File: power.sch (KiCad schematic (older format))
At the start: 44 parts, among them J11 Barrel_Jack_Switch, Q1 DMP2040USS, U10 TPS74401_VQFN, U11 LTC3633, U9 ISL8033A

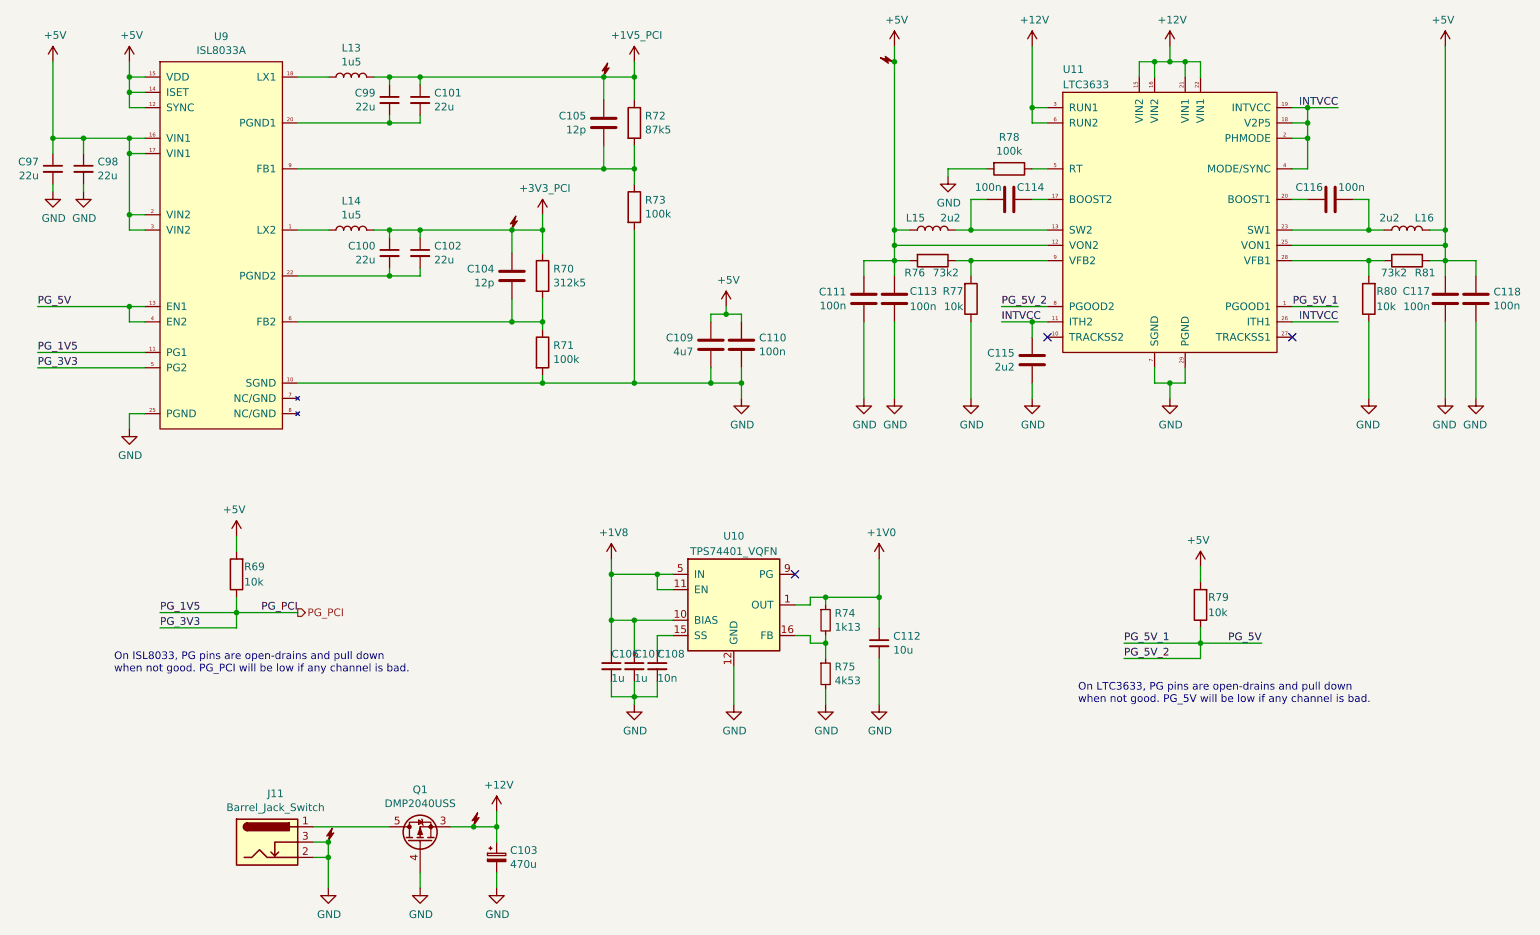
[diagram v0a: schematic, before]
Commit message: lib, sch: Fix connectors refdes letter
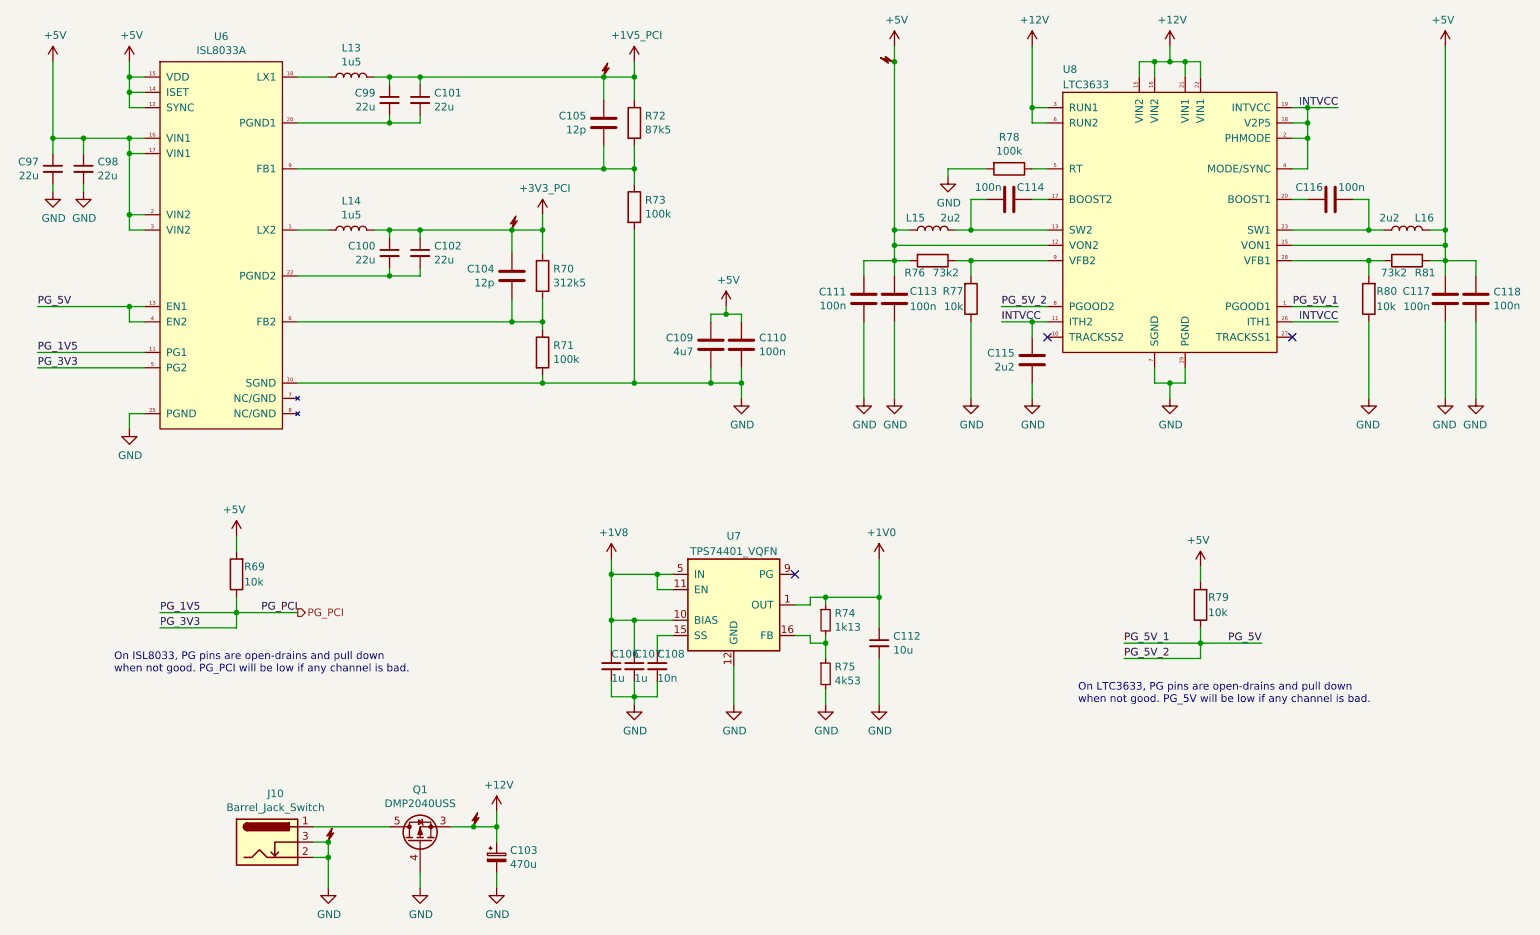
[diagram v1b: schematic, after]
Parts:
- renumbered J11 to J10, U9 to U6, U10 to U7, U11 to U8
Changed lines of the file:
@@
 $EndDescr
 $Comp
-L pimouss-motherboard:ISL8033A U9
+L pimouss-motherboard:ISL8033A U6
 U 1 1 5D0C46C4
 P 2000 1700
-F 0 "U9" H 2400 1865 50  0000 C CNN
+F 0 "U6" H 2400 1865 50  0000 C CNN
 F 1 "ISL8033A" H 2400 1774 50  0000 C CNN
 F 2 "Package_DFN_QFN:QFN-24-1EP_4x4mm_P0.5mm_EP2.6x2.6mm" H 3200 -800 50  0001 C CNN
@@
 	5700 3350 5800 3350
 $Comp
-L pimouss-motherboard:LTC3633 U11
+L pimouss-motherboard:LTC3633 U8
 U 1 1 5D19DF15
 P 7900 1900
-F 0 "U11" H 7900 2050 50  0000 L CNN
+F 0 "U8" H 7900 2050 50  0000 L CNN
 F 1 "LTC3633" H 7900 1950 50  0000 L CNN
 F 2 "Package_DFN_QFN:QFN-28-1EP_4x5mm_P0.5mm_EP2.65x3.65mm_ThermalVias" H 7800 1950 50  0001 C CNN
@@
 PG_PCI
 $Comp
-L Connector:Barrel_Jack_Switch J11
+L Connector:Barrel_Jack_Switch J10
 U 1 1 5D2C9CDF
 P 2700 6800
-F 0 "J11" H 2755 7117 50  0000 C CNN
+F 0 "J10" H 2755 7117 50  0000 C CNN
 F 1 "Barrel_Jack_Switch" H 2755 7026 50  0000 C CNN
 F 2 "Connector_BarrelJack:BarrelJack_Horizontal" H 2750 6760 50  0001 C CNN
@@
 	4200 7000 4200 7100
 $Comp
-L pimouss-motherboard:TPS74401_VQFN U10
+L pimouss-motherboard:TPS74401_VQFN U7
 U 1 1 5CE43F9B
 P 5450 4950
-F 0 "U10" H 5750 5100 50  0000 C CNN
+F 0 "U7" H 5750 5100 50  0000 C CNN
 F 1 "TPS74401_VQFN" H 5750 5000 50  0000 C CNN
 F 2 "Package_DFN_QFN:Texas_S-PVQFN-N20_EP3.15x3.15mm_ThermalVias" H 6250 4350 50  0001 C CNN

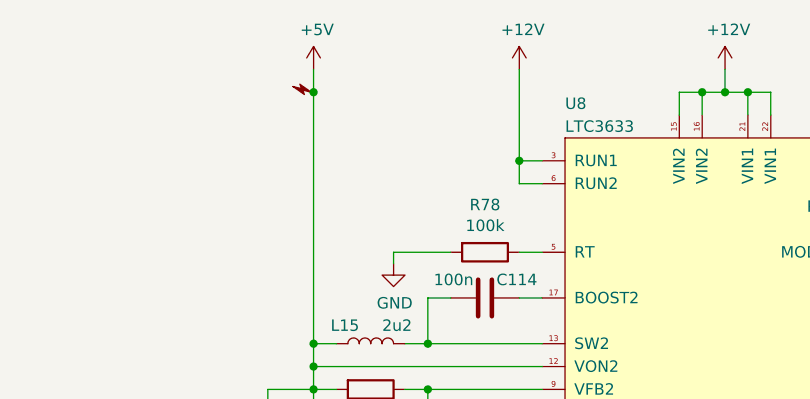
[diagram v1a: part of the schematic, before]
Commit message: sch/power: Add main 5V buck input decoupling caps
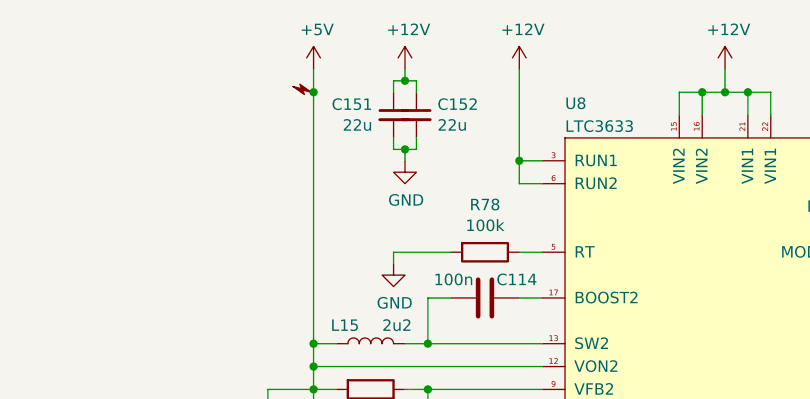
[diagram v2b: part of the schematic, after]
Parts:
- added C151, C152: 22u, Capacitor_SMD:C_0805_2012Metric, symbol Device:C_Small
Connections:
- net +12V: now also C151.1, C152.1
- net GND: now also C151.2, C152.2
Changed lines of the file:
@@
 	3000 6700 3500 6700
 Connection ~ 3100 6800
+$Comp
+L Device:C_Small C151
+U 1 1 5D0A7969
+P 7150 1800
+F 0 "C151" H 7058 1846 50  0000 R CNN
+F 1 "22u" H 7058 1755 50  0000 R CNN
+F 2 "Capacitor_SMD:C_0805_2012Metric" H 7150 1800 50  0001 C CNN
+F 3 "~" H 7150 1800 50  0001 C CNN
+	1    7150 1800
+	1    0    0    -1
+$EndComp
+$Comp
+L Device:C_Small C152
+U 1 1 5D0AA57C
+P 7250 1800
+F 0 "C152" H 7342 1846 50  0000 L CNN
+F 1 "22u" H 7342 1755 50  0000 L CNN
+F 2 "Capacitor_SMD:C_0805_2012Metric" H 7250 1800 50  0001 C CNN
+F 3 "~" H 7250 1800 50  0001 C CNN
+	1    7250 1800
+	1    0    0    -1
+$EndComp
+Wire Wire Line
+	7150 1700 7150 1650
+Wire Wire Line
+	7150 1650 7200 1650
+Wire Wire Line
+	7250 1650 7250 1700
+Wire Wire Line
+	7200 1650 7200 1600
+Connection ~ 7200 1650
+Wire Wire Line
+	7200 1650 7250 1650
+Wire Wire Line
+	7150 1900 7150 1950
+Wire Wire Line
+	7150 1950 7200 1950
+Wire Wire Line
+	7250 1950 7250 1900
+Wire Wire Line
+	7200 1950 7200 2000
+Connection ~ 7200 1950
+Wire Wire Line
+	7200 1950 7250 1950
+$Comp
+L power:+12V #PWR0193
+U 1 1 5D11D181
+P 7200 1600
+F 0 "#PWR0193" H 7200 1450 50  0001 C CNN
+F 1 "+12V" H 7215 1773 50  0000 C CNN
+F 2 "" H 7200 1600 50  0001 C CNN
+F 3 "" H 7200 1600 50  0001 C CNN
+	1    7200 1600
+	1    0    0    -1
+$EndComp
+$Comp
+L power:GND #PWR0194
+U 1 1 5D11D697
+P 7200 2000
+F 0 "#PWR0194" H 7200 1750 50  0001 C CNN
+F 1 "GND" H 7205 1827 50  0000 C CNN
+F 2 "" H 7200 2000 50  0001 C CNN
+F 3 "" H 7200 2000 50  0001 C CNN
+	1    7200 2000
+	1    0    0    -1
+$EndComp
 $EndSCHEMATC

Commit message: lib: Remove LTC3633 stupid bottom layer thermal pad
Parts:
- U8: footprint Package_DFN_QFN:QFN-28-1EP_4x5mm_P0.5mm_EP2.65x3.65mm_ThermalVias -> pimouss-motherboard:QFN-28-1EP_4x5mm_P0.5mm_EP2.65x3.65mm_ThermalVias
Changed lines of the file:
@@
 F 0 "U8" H 7900 2050 50  0000 L CNN
 F 1 "LTC3633" H 7900 1950 50  0000 L CNN
-F 2 "Package_DFN_QFN:QFN-28-1EP_4x5mm_P0.5mm_EP2.65x3.65mm_ThermalVias" H 7800 1950 50  0001 C CNN
+F 2 "pimouss-motherboard:QFN-28-1EP_4x5mm_P0.5mm_EP2.65x3.65mm_ThermalVias" H 7800 1950 50  0001 C CNN
 F 3 "https://www.analog.com/media/en/technical-documentation/data-sheets/3633fd.pdf" H 7900 2050 50  0001 C CNN
 	1    7900 1900

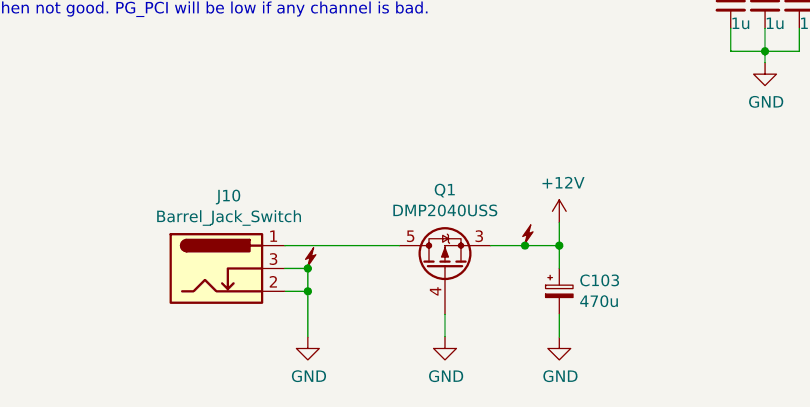
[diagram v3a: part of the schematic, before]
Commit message: sch: Simplify PSU
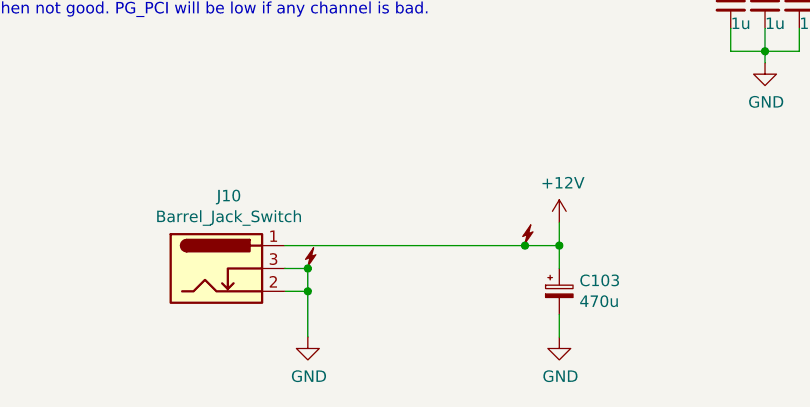
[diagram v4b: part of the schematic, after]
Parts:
- removed Q1: DMP2040USS, Package_SO:SOIC-8_3.9x4.9mm_P1.27mm, symbol pimouss-motherboard:DMP2040USS
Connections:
- net +12V: now also J10.1
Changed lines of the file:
@@
 Connection ~ 3100 6900
-$Comp
-L pimouss-motherboard:DMP2040USS Q1
-U 1 1 5D2E0A7B
-P 3700 6800
-F 0 "Q1" V 4043 6800 50  0000 C CNN
-F 1 "DMP2040USS" V 3952 6800 50  0000 C CNN
-F 2 "Package_SO:SOIC-8_3.9x4.9mm_P1.27mm" H 3900 6900 50  0001 C CNN
-F 3 "https://www.diodes.com/assets/Datasheets/DMP2040USS.pdf" H 3700 6800 50  0001 C CNN
-	1    3700 6800
-	0    -1   -1   0
-$EndComp
-$Comp
-L power:GND #PWR0160
-U 1 1 5D2EFEF0
-P 3700 7100
-F 0 "#PWR0160" H 3700 6850 50  0001 C CNN
-F 1 "GND" H 3705 6927 50  0000 C CNN
-F 2 "" H 3700 7100 50  0001 C CNN
-F 3 "" H 3700 7100 50  0001 C CNN
-	1    3700 7100
-	1    0    0    -1
-$EndComp
-Wire Wire Line
-	3700 7000 3700 7100
 $Comp
 L Device:CP_Small C103
@@
 Wire Wire Line
 	7300 2800 7800 2800
-Wire Wire Line
-	3900 6700 4050 6700
 $Comp
 L pimouss-motherboard:DummySupply #DS?
@@
 	1    0    0    -1
 $EndComp
-Connection ~ 4050 6700
 Wire Wire Line
 	4050 6700 4200 6700
-Wire Wire Line
-	3000 6700 3500 6700
 Connection ~ 3100 6800
 $Comp
@@
 	1    0    0    -1
 $EndComp
+Wire Wire Line
+	3000 6700 4050 6700
+Connection ~ 4050 6700
 $EndSCHEMATC

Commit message: *: Fix TPS74401 thermal pad on bottom layer
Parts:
- U7: footprint Package_DFN_QFN:Texas_S-PVQFN-N20_EP3.15x3.15mm_ThermalVias -> pimouss-motherboard:Texas_S-PVQFN-N20_EP3.15x3.15mm_ThermalVias
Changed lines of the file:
@@
 F 0 "U7" H 5750 5100 50  0000 C CNN
 F 1 "TPS74401_VQFN" H 5750 5000 50  0000 C CNN
-F 2 "Package_DFN_QFN:Texas_S-PVQFN-N20_EP3.15x3.15mm_ThermalVias" H 6250 4350 50  0001 C CNN
+F 2 "pimouss-motherboard:Texas_S-PVQFN-N20_EP3.15x3.15mm_ThermalVias" H 6250 4350 50  0001 C CNN
 F 3 "http://www.ti.com/general/docs/lit/getliterature.tsp?genericPartNumber=tps74401&fileType=pdf" H 5450 5450 50  0001 C CNN
 	1    5450 4950

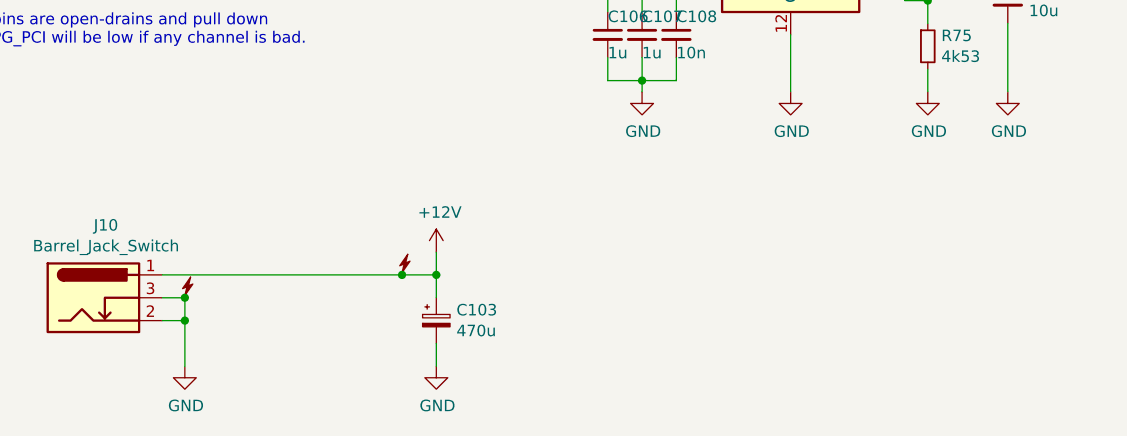
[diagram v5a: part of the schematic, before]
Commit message: pcb: Add more 12V caps
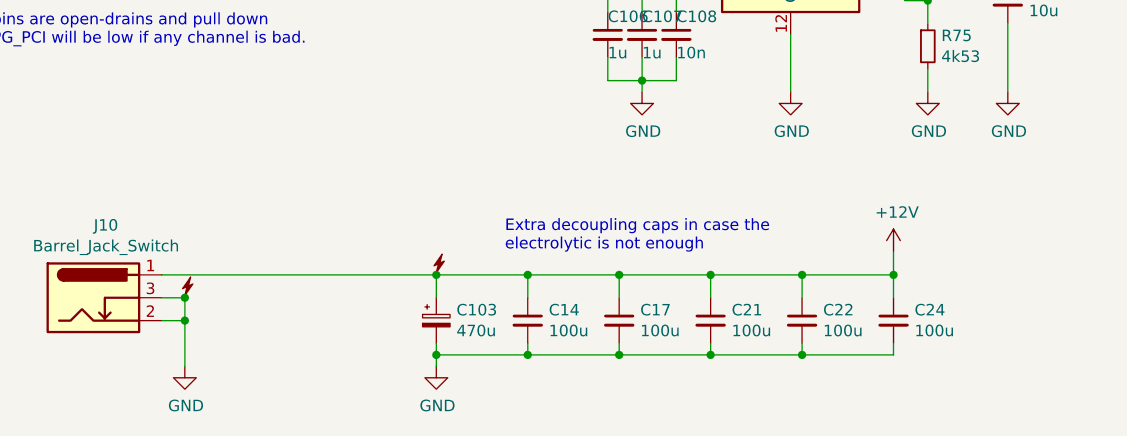
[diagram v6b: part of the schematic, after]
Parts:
- added C14, C17, C21, C22, C24: 100u, Capacitor_SMD:C_2220_5650Metric, symbol Device:C_Small
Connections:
- net +12V: now also C14.1, C17.1, C21.1, C22.1, C24.1
- net GND: now also C14.2, C17.2, C21.2, C22.2, C24.2
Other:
- note added: "Extra decoupling caps in case the\nelectrolytic is not enough"
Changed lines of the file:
@@
 L power:+12V #PWR0161
 U 1 1 5D3076B1
-P 4200 6600
-F 0 "#PWR0161" H 4200 6450 50  0001 C CNN
-F 1 "+12V" H 4215 6773 50  0000 C CNN
-F 2 "" H 4200 6600 50  0001 C CNN
-F 3 "" H 4200 6600 50  0001 C CNN
-	1    4200 6600
-	1    0    0    -1
-$EndComp
-Wire Wire Line
-	4200 6700 4200 6600
+P 6200 6600
+F 0 "#PWR0161" H 6200 6450 50  0001 C CNN
+F 1 "+12V" H 6215 6773 50  0000 C CNN
+F 2 "" H 6200 6600 50  0001 C CNN
+F 3 "" H 6200 6600 50  0001 C CNN
+	1    6200 6600
+	1    0    0    -1
+$EndComp
+Wire Wire Line
+	6200 6700 6200 6600
 Wire Wire Line
 	4200 6700 4200 6800
 Connection ~ 4200 6700
 Wire Wire Line
-	4200 7000 4200 7100
+	4200 7000 4200 7050
 $Comp
 L pimouss-motherboard:TPS74401_VQFN U7
@@
 L pimouss-motherboard:DummySupply #DS?
 U 1 1 5DE84E2B
-P 4050 6700
+P 4200 6700
 AR Path="/5DE84E2B" Ref="#DS?"  Part="1"
 AR Path="/5D0C4621/5DE84E2B" Ref="#DS018"  Part="1"
-F 0 "#DS018" H 4050 6700 50  0001 C CNN
-F 1 "DummySupply" H 4050 6700 50  0001 C CNN
-F 2 "" H 4050 6700 50  0001 C CNN
-F 3 "" H 4050 6700 50  0001 C CNN
-	1    4050 6700
-	1    0    0    -1
-$EndComp
-Wire Wire Line
-	4050 6700 4200 6700
+F 0 "#DS018" H 4200 6700 50  0001 C CNN
+F 1 "DummySupply" H 4200 6700 50  0001 C CNN
+F 2 "" H 4200 6700 50  0001 C CNN
+F 3 "" H 4200 6700 50  0001 C CNN
+	1    4200 6700
+	1    0    0    -1
+$EndComp
 Connection ~ 3100 6800
 $Comp
@@
 	1    0    0    -1
 $EndComp
-Wire Wire Line
-	3000 6700 4050 6700
-Connection ~ 4050 6700
+$Comp
+L Device:C_Small C14
+U 1 1 5D08FF87
+P 4600 6900
+F 0 "C14" H 4692 6946 50  0000 L CNN
+F 1 "100u" H 4692 6855 50  0000 L CNN
+F 2 "Capacitor_SMD:C_2220_5650Metric" H 4600 6900 50  0001 C CNN
+F 3 "~" H 4600 6900 50  0001 C CNN
+	1    4600 6900
+	1    0    0    -1
+$EndComp
+Text Notes 4500 6600 0    50   ~ 0
+Extra decoupling caps in case the\nelectrolytic is not enough
+$Comp
+L Device:C_Small C17
+U 1 1 5D0934B1
+P 5000 6900
+F 0 "C17" H 5092 6946 50  0000 L CNN
+F 1 "100u" H 5092 6855 50  0000 L CNN
+F 2 "Capacitor_SMD:C_2220_5650Metric" H 5000 6900 50  0001 C CNN
+F 3 "~" H 5000 6900 50  0001 C CNN
+	1    5000 6900
+	1    0    0    -1
+$EndComp
+$Comp
+L Device:C_Small C21
+U 1 1 5D093DB2
+P 5400 6900
+F 0 "C21" H 5492 6946 50  0000 L CNN
+F 1 "100u" H 5492 6855 50  0000 L CNN
+F 2 "Capacitor_SMD:C_2220_5650Metric" H 5400 6900 50  0001 C CNN
+F 3 "~" H 5400 6900 50  0001 C CNN
+	1    5400 6900
+	1    0    0    -1
+$EndComp
+$Comp
+L Device:C_Small C22
+U 1 1 5D09430E
+P 5800 6900
+F 0 "C22" H 5892 6946 50  0000 L CNN
+F 1 "100u" H 5892 6855 50  0000 L CNN
+F 2 "Capacitor_SMD:C_2220_5650Metric" H 5800 6900 50  0001 C CNN
+F 3 "~" H 5800 6900 50  0001 C CNN
+	1    5800 6900
+	1    0    0    -1
+$EndComp
+$Comp
+L Device:C_Small C24
+U 1 1 5D094AB5
+P 6200 6900
+F 0 "C24" H 6292 6946 50  0000 L CNN
+F 1 "100u" H 6292 6855 50  0000 L CNN
+F 2 "Capacitor_SMD:C_2220_5650Metric" H 6200 6900 50  0001 C CNN
+F 3 "~" H 6200 6900 50  0001 C CNN
+	1    6200 6900
+	1    0    0    -1
+$EndComp
+Wire Wire Line
+	4200 6700 4600 6700
+Wire Wire Line
+	6200 6700 6200 6800
+Wire Wire Line
+	4600 6800 4600 6700
+Connection ~ 4600 6700
+Wire Wire Line
+	4600 6700 5000 6700
+Wire Wire Line
+	5000 6800 5000 6700
+Connection ~ 5000 6700
+Wire Wire Line
+	5000 6700 5400 6700
+Wire Wire Line
+	5400 6800 5400 6700
+Connection ~ 5400 6700
+Wire Wire Line
+	5400 6700 5800 6700
+Wire Wire Line
+	5800 6800 5800 6700
+Connection ~ 5800 6700
+Wire Wire Line
+	5800 6700 6200 6700
+Wire Wire Line
+	4200 7050 4600 7050
+Wire Wire Line
+	6200 7050 6200 7000
+Connection ~ 4200 7050
+Wire Wire Line
+	4200 7050 4200 7100
+Wire Wire Line
+	4600 7000 4600 7050
+Connection ~ 4600 7050
+Wire Wire Line
+	4600 7050 5000 7050
+Wire Wire Line
+	5000 7000 5000 7050
+Connection ~ 5000 7050
+Wire Wire Line
+	5000 7050 5400 7050
+Wire Wire Line
+	5400 7000 5400 7050
+Connection ~ 5400 7050
+Wire Wire Line
+	5400 7050 5800 7050
+Wire Wire Line
+	5800 7000 5800 7050
+Connection ~ 5800 7050
+Wire Wire Line
+	5800 7050 6200 7050
+Connection ~ 6200 6700
+Wire Wire Line
+	3000 6700 4200 6700
 $EndSCHEMATC
